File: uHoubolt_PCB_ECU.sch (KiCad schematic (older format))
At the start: 80 parts, among them J1 Power In, J2 Debug, J24 12V, J25 GND, J26 Servo, J3 CAN1, J35 CAN1, J36 CAN2, J37 CAN1, J38 CAN2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

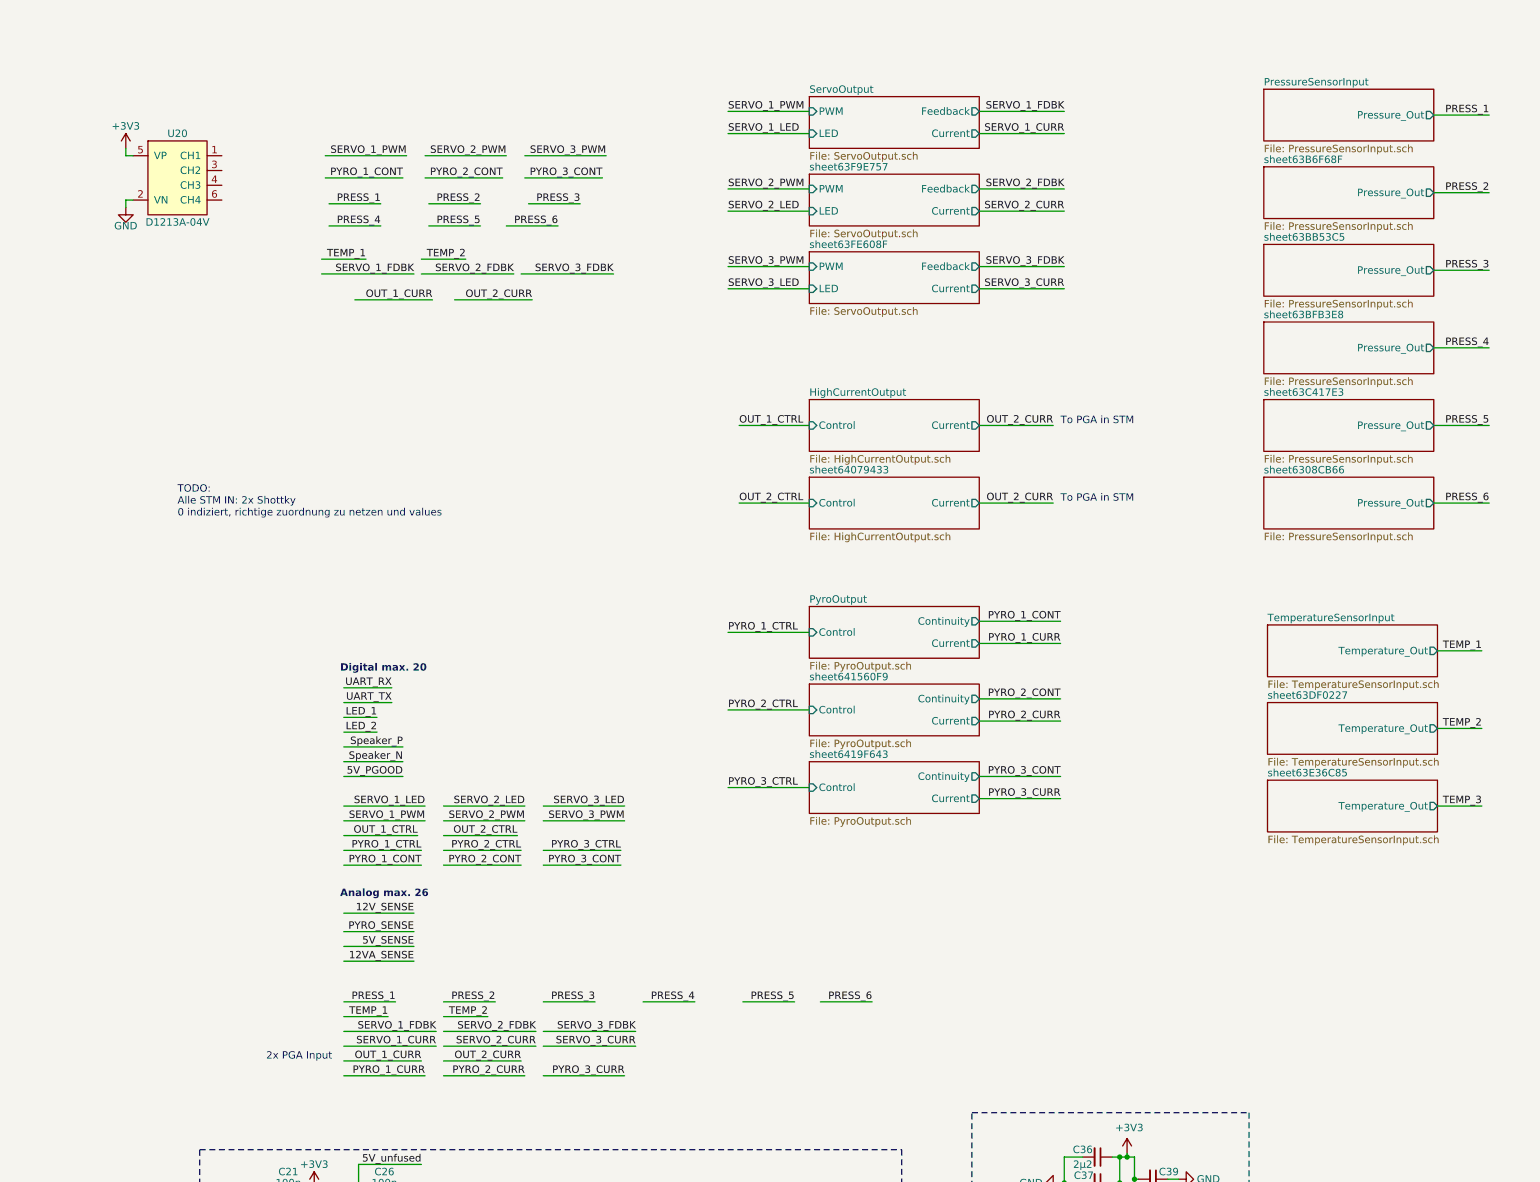
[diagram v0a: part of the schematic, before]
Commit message: fixed net names
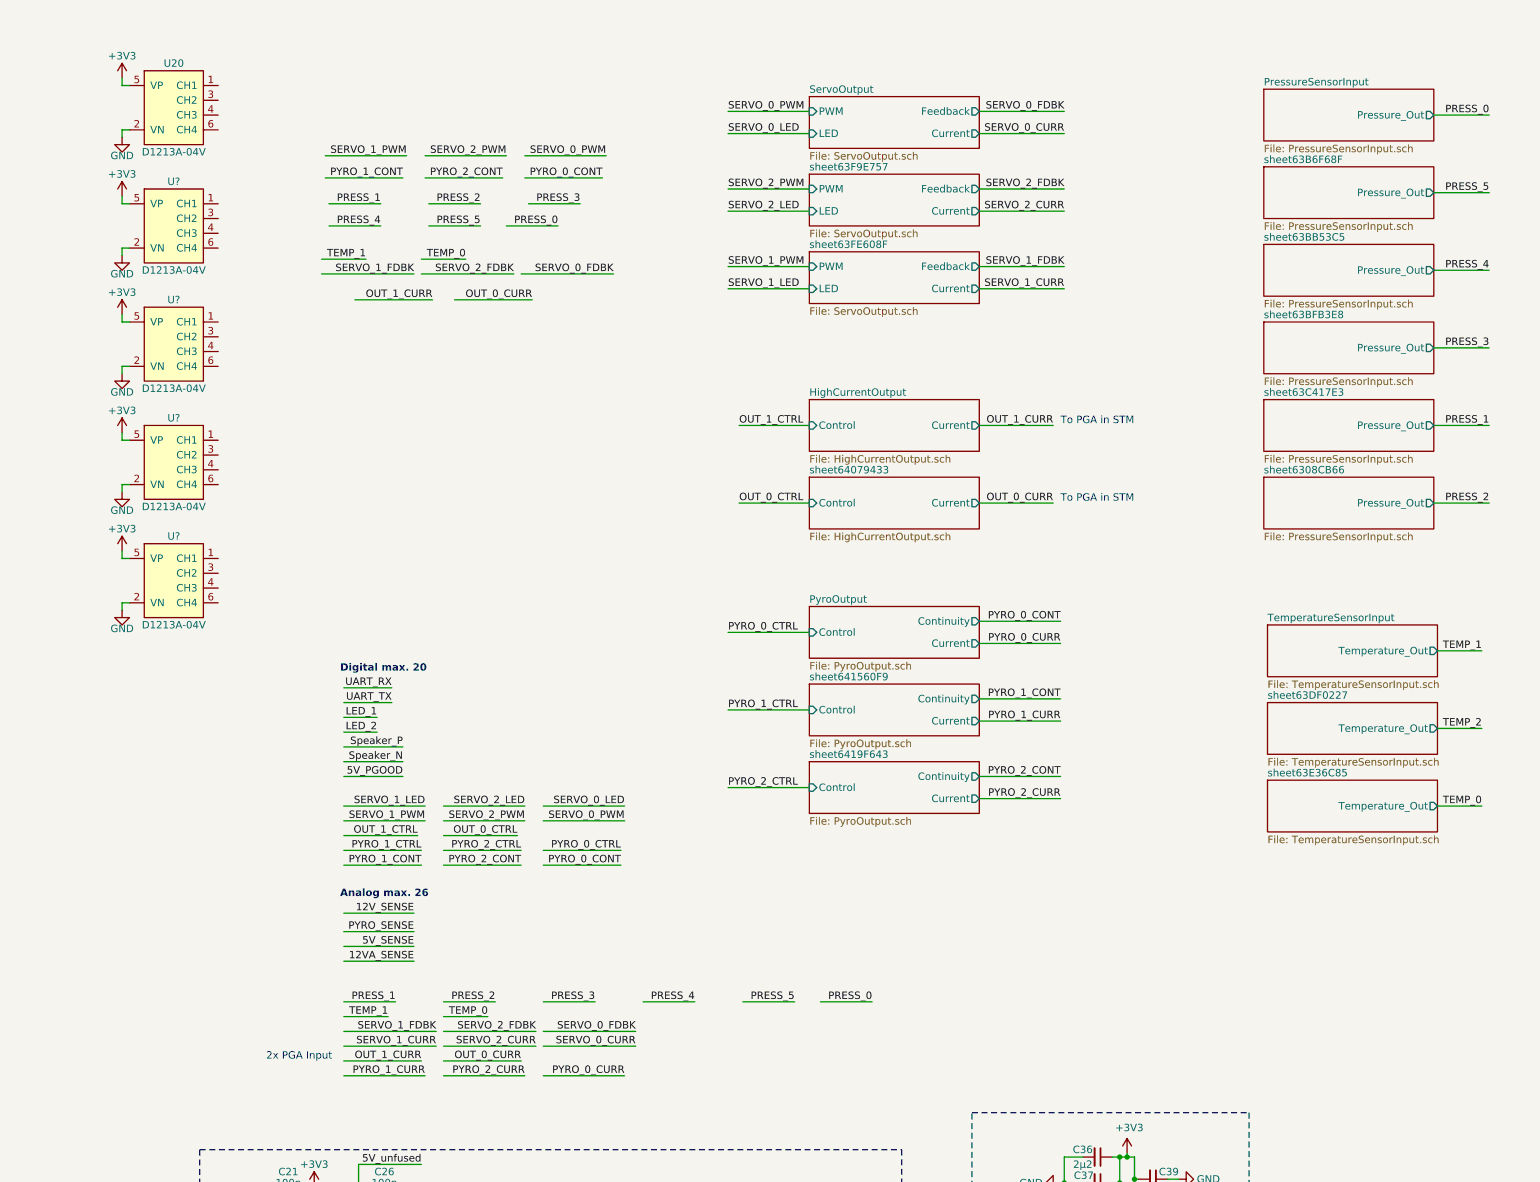
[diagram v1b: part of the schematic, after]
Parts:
- added U? (x4): D1213A-04V, Package_TO_SOT_SMD:SOT-563, symbol TXV_LIB:D1213A-04V
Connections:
- net labels added: OUT_0_CTRL, OUT_0_CURR, PRESS_0, PYRO_0_CONT, PYRO_0_CTRL, PYRO_0_CURR, SERVO_0_CURR, SERVO_0_FDBK, SERVO_0_LED, SERVO_0_PWM, TEMP_0
- net labels removed: OUT_2_CTRL, OUT_2_CURR, PRESS_6, PYRO_3_CONT, PYRO_3_CTRL, PYRO_3_CURR, SERVO_3_CURR, SERVO_3_FDBK, SERVO_3_LED, SERVO_3_PWM, TEMP_3
- wire segments 484 -> 500
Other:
- note removed: "TODO:\nAlle STM IN: 2x Shottky\n0 indiziert, richtige zuordnung zu netzen und values"
- moved on the sheet: U20

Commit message: schematic done, preliminary placement done
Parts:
- added Q3: SISA88DN or similar, TXV_LIB:PowerPAK_1212-8, symbol Device:Q_NMOS_GDS
- added R77: 120, Resistor_SMD:R_0603_1608Metric, symbol Device:R_Small
- added R78: 1k, Resistor_SMD:R_0603_1608Metric, symbol Device:R_Small
- gave numbers to parts that had none: 4
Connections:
- net labels added: SOLENOID_0_CTRL, SOLENOID_0_CURR, SOLENOID_1_CTRL, SOLENOID_1_CURR, Speaker
- net labels removed: OUT_0_CTRL, OUT_0_CURR, OUT_1_CTRL, OUT_1_CURR, Speaker_N, Speaker_P
- wire segments 500 -> 525
- no-connect marks 3 -> 5
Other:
- note added: "PGA"
- note added: "PGA Inverting In"
- note removed: "2x PGA Input"
- note removed: "Analog max. 26"
- note removed: "Digital max. 20"
- moved on the sheet: D4, D5, J2, LS1, R19, R20

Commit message: routing started
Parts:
- J1: footprint TXV_LIB:Molex_MegaFit_1x03_Vertical -> TXV_LIB:Molex_MegaFit_1x03_Vertical_Doublesided
- U20, U21, U22, U23, U24: footprint Package_TO_SOT_SMD:SOT-563 -> TXV_LIB:SOT-563
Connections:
- net +12V: now also LS1.1, R78.1
- net +12VA: no longer LS1.1, R78.1
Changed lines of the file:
@@
 F 0 "J1" H 775 1425 50  0000 C CNN
 F 1 "Power In" H 775 1350 50  0000 C CNN
-F 2 "TXV_LIB:Molex_MegaFit_1x03_Vertical" H 775 1150 50  0001 C CNN
+F 2 "TXV_LIB:Molex_MegaFit_1x03_Vertical_Doublesided" H 775 1150 50  0001 C CNN
 F 3 "~" H 775 1150 50  0001 C CNN
 	1    775  1150
@@
 F 0 "U20" H 6800 1500 50  0000 C CNN
 F 1 "D1213A-04V" H 6800 900 50  0000 C CNN
-F 2 "Package_TO_SOT_SMD:SOT-563" H 6800 800 50  0001 C CNN
+F 2 "TXV_LIB:SOT-563" H 6800 800 50  0001 C CNN
 F 3 "" H 6800 1200 50  0001 C CNN
 	1    6800 1200
@@
 F 0 "U21" H 6800 2300 50  0000 C CNN
 F 1 "D1213A-04V" H 6800 1700 50  0000 C CNN
-F 2 "Package_TO_SOT_SMD:SOT-563" H 6800 1600 50  0001 C CNN
+F 2 "TXV_LIB:SOT-563" H 6800 1600 50  0001 C CNN
 F 3 "" H 6800 2000 50  0001 C CNN
 	1    6800 2000
@@
 F 0 "U22" H 6800 3100 50  0000 C CNN
 F 1 "D1213A-04V" H 6800 2500 50  0000 C CNN
-F 2 "Package_TO_SOT_SMD:SOT-563" H 6800 2400 50  0001 C CNN
+F 2 "TXV_LIB:SOT-563" H 6800 2400 50  0001 C CNN
 F 3 "" H 6800 2800 50  0001 C CNN
 	1    6800 2800
@@
 F 0 "U23" H 6800 3900 50  0000 C CNN
 F 1 "D1213A-04V" H 6800 3300 50  0000 C CNN
-F 2 "Package_TO_SOT_SMD:SOT-563" H 6800 3200 50  0001 C CNN
+F 2 "TXV_LIB:SOT-563" H 6800 3200 50  0001 C CNN
 F 3 "" H 6800 3600 50  0001 C CNN
 	1    6800 3600
@@
 F 0 "U24" H 6800 4700 50  0000 C CNN
 F 1 "D1213A-04V" H 6800 4100 50  0000 C CNN
-F 2 "Package_TO_SOT_SMD:SOT-563" H 6800 4000 50  0001 C CNN
+F 2 "TXV_LIB:SOT-563" H 6800 4000 50  0001 C CNN
 F 3 "" H 6800 4400 50  0001 C CNN
 	1    6800 4400
@@
 	4475 4375 4525 4375
 $Comp
-L power:+12VA #PWR0228
-U 1 1 658F8B5D
-P 4475 4200
-F 0 "#PWR0228" H 4475 4050 50  0001 C CNN
-F 1 "+12VA" H 4475 4350 50  0000 C CNN
-F 2 "" H 4475 4200 50  0001 C CNN
-F 3 "" H 4475 4200 50  0001 C CNN
-	1    4475 4200
-	1    0    0    -1
-$EndComp
-$Comp
 L Device:R_Small R77
 U 1 1 6594F65C
@@
 	3050 1375 3050 1400
 Connection ~ 3050 1400
+$Comp
+L power:+12V #PWR?
+U 1 1 61D3A685
+P 4475 4200
+F 0 "#PWR?" H 4475 4050 50  0001 C CNN
+F 1 "+12V" H 4475 4350 50  0000 C CNN
+F 2 "" H 4475 4200 50  0001 C CNN
+F 3 "" H 4475 4200 50  0001 C CNN
+	1    4475 4200
+	1    0    0    -1
+$EndComp
 $EndSCHEMATC

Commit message: routing done, drc clean (3 errors to be ignored)
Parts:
- removed J24: 12V, TXV_LIB:PlatedEdgePad_6mm, symbol Connector_Generic:Conn_01x01
- removed J25: GND, TXV_LIB:PlatedEdgePad_6mm, symbol Connector_Generic:Conn_01x01
- removed J26: Servo, TXV_LIB:PlatedEdgePad_6mm, symbol Connector_Generic:Conn_01x01
- added JP2: Servo Voltage Select, TXV_LIB:Jumper3_6x2mm_Vias23, symbol Jumper:SolderJumper_3_Open
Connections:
- net +12V: now also JP2.2 (C)
- net GND: now also U8.9 (PAD), JP2.3 (B)
- net SOLENOID_0_CTRL: now also U6.48 (PD9); no longer U6.47 (PD8)
- net SOLENOID_0_CURR: now also U6.21 (PA7); no longer U6.24 (PB0)
- net SOLENOID_1_CTRL: now also U6.47 (PD8); no longer U6.48 (PD9)
- net SOLENOID_1_CURR: now also U6.24 (PB0); no longer U6.21 (PA7)
- net VS: now also JP2.1 (A)
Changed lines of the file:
@@
 L power:GND #PWR?
 U 1 1 63229F21
-P 3625 10750
+P 3625 10775
 AR Path="/6015C35D/63229F21" Ref="#PWR?"  Part="1"
 AR Path="/63229F21" Ref="#PWR052"  Part="1"
-F 0 "#PWR052" H 3625 10500 50  0001 C CNN
-F 1 "GND" H 3630 10577 50  0000 C CNN
-F 2 "" H 3625 10750 50  0001 C CNN
-F 3 "" H 3625 10750 50  0001 C CNN
-	1    3625 10750
+F 0 "#PWR052" H 3625 10525 50  0001 C CNN
+F 1 "GND" H 3630 10602 50  0000 C CNN
+F 2 "" H 3625 10775 50  0001 C CNN
+F 3 "" H 3625 10775 50  0001 C CNN
+	1    3625 10775
 	1    0    0    -1
 $EndComp
@@
 	2900 8925 2350 8925
 Wire Wire Line
-	5300 6925 4600 6925
-Text Label 5300 6925 2    50   ~ 0
+	5300 7025 4600 7025
+Text Label 5300 7025 2    50   ~ 0
 SOLENOID_1_CTRL
 Text Label 5125 7725 2    50   ~ 0
@@
 	2900 9025 2350 9025
 Wire Wire Line
-	5300 7025 4600 7025
-Text Label 5300 7025 2    50   ~ 0
+	5300 6925 4600 6925
+Text Label 5300 6925 2    50   ~ 0
 SOLENOID_0_CTRL
 Text Label 5125 7925 2    50   ~ 0
@@
 Text Label 5150 6725 2    50   ~ 0
 PYRO_2_CURR
-Text Label 2175 8125 0    50   ~ 0
-SOLENOID_0_CURR
 Wire Wire Line
 	2900 6925 2275 6925
@@
 L power:VS #PWR0101
 U 1 1 62FBA5C0
-P 3875 775
-F 0 "#PWR0101" H 3675 625 50  0001 C CNN
-F 1 "VS" H 3875 925 50  0000 C CNN
-F 2 "" H 3875 775 50  0001 C CNN
-F 3 "" H 3875 775 50  0001 C CNN
-	1    3875 775
-	1    0    0    -1
-$EndComp
-$Comp
-L power:+12V #PWR?
-U 1 1 62FBB19F
-P 3475 800
-AR Path="/61C7474C/62FBB19F" Ref="#PWR?"  Part="1"
-AR Path="/62FBB19F" Ref="#PWR0102"  Part="1"
-F 0 "#PWR0102" H 3475 650 50  0001 C CNN
-F 1 "+12V" H 3475 950 50  0000 C CNN
-F 2 "" H 3475 800 50  0001 C CNN
-F 3 "" H 3475 800 50  0001 C CNN
-	1    3475 800
+P 3925 750
+F 0 "#PWR0101" H 3725 600 50  0001 C CNN
+F 1 "VS" H 3925 900 50  0000 C CNN
+F 2 "" H 3925 750 50  0001 C CNN
+F 3 "" H 3925 750 50  0001 C CNN
+	1    3925 750
 	1    0    0    -1
 $EndComp
@@
 Wire Wire Line
 	6450 1350 6450 1400
-$Comp
-L Connector_Generic:Conn_01x01 J24
-U 1 1 63187D15
-P 3475 1025
-F 0 "J24" V 3375 1025 50  0000 L CNN
-F 1 "12V" V 3575 950 50  0000 L CNN
-F 2 "TXV_LIB:PlatedEdgePad_6mm" H 3475 1025 50  0001 C CNN
-F 3 "~" H 3475 1025 50  0001 C CNN
-	1    3475 1025
-	0    1    1    0
-$EndComp
-$Comp
-L Connector_Generic:Conn_01x01 J26
-U 1 1 6318DCA6
-P 3875 1025
-F 0 "J26" V 3825 825 50  0000 L CNN
-F 1 "Servo" V 3975 925 50  0000 L CNN
-F 2 "TXV_LIB:PlatedEdgePad_6mm" H 3875 1025 50  0001 C CNN
-F 3 "~" H 3875 1025 50  0001 C CNN
-	1    3875 1025
-	0    1    1    0
-$EndComp
-$Comp
-L Connector_Generic:Conn_01x01 J25
-U 1 1 6318E212
-P 3675 750
-F 0 "J25" V 3575 725 50  0000 R CNN
-F 1 "GND" V 3775 825 50  0000 R CNN
-F 2 "TXV_LIB:PlatedEdgePad_6mm" H 3675 750 50  0001 C CNN
-F 3 "~" H 3675 750 50  0001 C CNN
-	1    3675 750
-	0    -1   -1   0
-$EndComp
-$Comp
-L power:GND #PWR0208
-U 1 1 6318F78B
-P 3675 975
-F 0 "#PWR0208" H 3675 725 50  0001 C CNN
-F 1 "GND" H 3675 825 50  0000 C CNN
-F 2 "" H 3675 975 50  0001 C CNN
-F 3 "" H 3675 975 50  0001 C CNN
-	1    3675 975
-	-1   0    0    -1
-$EndComp
-Wire Wire Line
-	3475 800  3475 825
-Wire Wire Line
-	3675 950  3675 975
-Wire Wire Line
-	3875 775  3875 800
 Text Label 10550 1375 0    50   ~ 0
 SERVO_0_LED
@@
 Text Notes 3200 8350 0    50   ~ 0
 PGA Inverting In
-Wire Wire Line
-	2900 8125 2175 8125
-Wire Wire Line
-	2900 7225 2175 7225
-Text Label 2175 7225 0    50   ~ 0
-SOLENOID_1_CURR
 Text Notes 3200 7250 0    50   ~ 0
 PGA
@@
 L power:PWR_FLAG #FLG0103
 U 1 1 67327E1F
-P 4000 775
-F 0 "#FLG0103" H 4000 850 50  0001 C CNN
-F 1 "PWR_FLAG" H 4000 925 50  0000 C CNN
-F 2 "" H 4000 775 50  0001 C CNN
-F 3 "~" H 4000 775 50  0001 C CNN
-	1    4000 775
-	1    0    0    -1
-$EndComp
-Wire Wire Line
-	4000 775  4000 800
-Wire Wire Line
-	4000 800  3875 800
-Connection ~ 3875 800
-Wire Wire Line
-	3875 800  3875 825
+P 4025 750
+F 0 "#FLG0103" H 4025 825 50  0001 C CNN
+F 1 "PWR_FLAG" V 4100 750 50  0000 C CNN
+F 2 "" H 4025 750 50  0001 C CNN
+F 3 "~" H 4025 750 50  0001 C CNN
+	1    4025 750
+	1    0    0    -1
+$EndComp
 $Comp
 L power:PWR_FLAG #FLG0104
@@
 Connection ~ 3050 1400
 $Comp
-L power:+12V #PWR?
+L power:+12V #PWR0102
 U 1 1 61D3A685
 P 4475 4200
-F 0 "#PWR?" H 4475 4050 50  0001 C CNN
+F 0 "#PWR0102" H 4475 4050 50  0001 C CNN
 F 1 "+12V" H 4475 4350 50  0000 C CNN
 F 2 "" H 4475 4200 50  0001 C CNN
@@
 	1    0    0    -1
 $EndComp
+$Comp
+L Jumper:SolderJumper_3_Open JP2
+U 1 1 61C315C6
+P 3700 925
+F 0 "JP2" H 3700 1038 50  0000 C CNN
+F 1 "Servo Voltage Select" H 3700 1175 50  0000 C CNN
+F 2 "TXV_LIB:Jumper3_6x2mm_Vias23" H 3700 925 50  0001 C CNN
+F 3 "~" H 3700 925 50  0001 C CNN
+	1    3700 925
+	-1   0    0    1
+$EndComp
+$Comp
+L power:+12V #PWR?
+U 1 1 61D2D8D1
+P 3700 750
+AR Path="/61C7474C/61D2D8D1" Ref="#PWR?"  Part="1"
+AR Path="/61D2D8D1" Ref="#PWR0208"  Part="1"
+F 0 "#PWR0208" H 3700 600 50  0001 C CNN
+F 1 "+12V" H 3700 900 50  0000 C CNN
+F 2 "" H 3700 750 50  0001 C CNN
+F 3 "" H 3700 750 50  0001 C CNN
+	1    3700 750
+	1    0    0    -1
+$EndComp
+$Comp
+L power:GND #PWR0228
+U 1 1 61DC6265
+P 3475 950
+F 0 "#PWR0228" H 3475 700 50  0001 C CNN
+F 1 "GND" H 3475 800 50  0000 C CNN
+F 2 "" H 3475 950 50  0001 C CNN
+F 3 "" H 3475 950 50  0001 C CNN
+	1    3475 950
+	1    0    0    -1
+$EndComp
+Wire Wire Line
+	3475 950  3475 925
+Wire Wire Line
+	3475 925  3500 925
+Wire Wire Line
+	3700 750  3700 775
+Wire Wire Line
+	3925 750  3925 800
+Wire Wire Line
+	3925 925  3900 925
+Wire Wire Line
+	4025 750  4025 800
+Wire Wire Line
+	4025 800  3925 800
+Connection ~ 3925 800
+Wire Wire Line
+	3925 800  3925 925
+Wire Wire Line
+	2900 7225 2175 7225
+Text Label 2175 7225 0    50   ~ 0
+SOLENOID_0_CURR
+Text Label 2175 8125 0    50   ~ 0
+SOLENOID_1_CURR
+Wire Wire Line
+	2900 8125 2175 8125
+Wire Wire Line
+	3475 10725 3475 10750
+Wire Wire Line
+	3475 10750 3625 10750
+Connection ~ 3625 10750
+Wire Wire Line
+	3625 10750 3625 10775
 $EndSCHEMATC

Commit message: small improvements, updated doc
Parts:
- added G1: SpaceTeam_LOGO, TXV_LIB:ST_Logo_new, symbol TXV_LIB:SpaceTeam_LOGO
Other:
- note added: "I/O Protection"
- note added: "Inputs & Outputs"
- moved on the sheet: C10, C12, C16, C17, C18, C19, C20, C21, C22, C23, C25, C26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

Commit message: small changes, generated gerbers
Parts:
- U4: value MCP2562FDT-H_SN -> MCP2562FDx-x_MF
- U5: value MCP2562FDT -> MCP2562FDx-x_MF
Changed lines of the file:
@@
 AR Path="/6322A0B2" Ref="U5"  Part="1"
 F 0 "U5" H 9375 8475 50  0000 C CNN
-F 1 "MCP2562FDT" H 9550 8550 50  0000 C CNN
+F 1 "MCP2562FDx-x_MF" H 9675 8550 50  0000 C CNN
 F 2 "Package_DFN_QFN:DFN-8-1EP_3x3mm_P0.65mm_EP1.55x2.4mm" H 9175 8400 50  0001 C CIN
 F 3 "http://ww1.microchip.com/downloads/en/DeviceDoc/25167A.pdf" H 9175 8900 50  0001 C CNN
@@
 AR Path="/6015C35D/6322A030" Ref="U?"  Part="1"
 AR Path="/6322A030" Ref="U4"  Part="1"
-F 0 "U4" H 9250 7000 50  0000 C CNN
-F 1 "MCP2562FDT-H_SN" H 9575 7100 50  0000 C CNN
+F 0 "U4" H 9350 7050 50  0000 C CNN
+F 1 "MCP2562FDx-x_MF" H 9650 7125 50  0000 C CNN
 F 2 "Package_DFN_QFN:DFN-8-1EP_3x3mm_P0.65mm_EP1.55x2.4mm" H 9175 6975 50  0001 C CIN
 F 3 "http://ww1.microchip.com/downloads/en/DeviceDoc/25167A.pdf" H 9175 7475 50  0001 C CNN

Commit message: some more small changes
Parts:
- R12, R4, R8: value 9k1 -> 56k
- R13, R5, R9: value 1k -> 10k
- R14, R15, R16: value 9k1 -> 10k
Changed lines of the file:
@@
 AR Path="/63229E9D" Ref="R16"  Part="1"
 F 0 "R16" V 1625 5350 50  0000 C CNN
-F 1 "9k1" V 1700 5350 50  0000 C CNN
+F 1 "10k" V 1700 5350 50  0000 C CNN
 F 2 "Resistor_SMD:R_0603_1608Metric" H 1775 5350 50  0001 C CNN
 F 3 "~" H 1775 5350 50  0001 C CNN
@@
 P 6325 2900
 F 0 "#FLG0102" H 6325 2975 50  0001 C CNN
-F 1 "PWR_FLAG" H 6325 3050 50  0000 C CNN
+F 1 "PWR_FLAG" V 6400 2975 50  0000 C CNN
 F 2 "" H 6325 2900 50  0001 C CNN
 F 3 "~" H 6325 2900 50  0001 C CNN
@@
 AR Path="/61C7474C/63A4C22D" Ref="#PWR?"  Part="1"
 F 0 "#PWR0218" H 9775 2100 50  0001 C CNN
-F 1 "+3V3" H 9790 2423 50  0000 C CNN
+F 1 "+3V3" H 9775 2400 50  0000 C CNN
 F 2 "" H 9775 2250 50  0001 C CNN
 F 3 "" H 9775 2250 50  0001 C CNN
@@
 U 1 1 635C8D87
 P 6225 3125
-F 0 "R12" H 6075 3175 50  0000 L CNN
-F 1 "9k1" H 6050 3100 50  0000 L CNN
+F 0 "R12" H 6050 3175 50  0000 L CNN
+F 1 "56k" H 6050 3100 50  0000 L CNN
 F 2 "Resistor_SMD:R_0603_1608Metric" H 6225 3125 50  0001 C CNN
 F 3 "~" H 6225 3125 50  0001 C CNN
@@
 U 1 1 635C8D81
 P 6225 3425
-F 0 "R13" H 6075 3450 50  0000 L CNN
-F 1 "1k" H 6075 3375 50  0000 L CNN
+F 0 "R13" H 6050 3450 50  0000 L CNN
+F 1 "10k" H 6075 3375 50  0000 L CNN
 F 2 "Resistor_SMD:R_0603_1608Metric" H 6225 3425 50  0001 C CNN
 F 3 "~" H 6225 3425 50  0001 C CNN
@@
 P 6950 1125
 F 0 "R4" H 6800 1175 50  0000 L CNN
-F 1 "9k1" H 6775 1100 50  0000 L CNN
+F 1 "56k" H 6775 1100 50  0000 L CNN
 F 2 "Resistor_SMD:R_0603_1608Metric" H 6950 1125 50  0001 C CNN
 F 3 "~" H 6950 1125 50  0001 C CNN
@@
 P 6950 1425
 F 0 "R5" H 6800 1450 50  0000 L CNN
-F 1 "1k" H 6800 1375 50  0000 L CNN
+F 1 "10k" H 6750 1375 50  0000 L CNN
 F 2 "Resistor_SMD:R_0603_1608Metric" H 6950 1425 50  0001 C CNN
 F 3 "~" H 6950 1425 50  0001 C CNN
@@
 P 7800 1125
 F 0 "R8" H 7650 1175 50  0000 L CNN
-F 1 "9k1" H 7625 1100 50  0000 L CNN
+F 1 "56k" H 7625 1100 50  0000 L CNN
 F 2 "Resistor_SMD:R_0603_1608Metric" H 7800 1125 50  0001 C CNN
 F 3 "~" H 7800 1125 50  0001 C CNN
@@
 P 7800 1425
 F 0 "R9" H 7650 1450 50  0000 L CNN
-F 1 "1k" H 7650 1375 50  0000 L CNN
+F 1 "10k" H 7600 1375 50  0000 L CNN
 F 2 "Resistor_SMD:R_0603_1608Metric" H 7800 1425 50  0001 C CNN
 F 3 "~" H 7800 1425 50  0001 C CNN
@@
 P 9025 2675
 F 0 "R14" H 8825 2725 50  0000 L CNN
-F 1 "9k1" H 8825 2650 50  0000 L CNN
+F 1 "10k" H 8825 2650 50  0000 L CNN
 F 2 "Resistor_SMD:R_0603_1608Metric" H 9025 2675 50  0001 C CNN
 F 3 "~" H 9025 2675 50  0001 C CNN
@@
 P 9025 2925
 F 0 "R15" H 8825 2950 50  0000 L CNN
-F 1 "9k1" H 8825 2875 50  0000 L CNN
+F 1 "10k" H 8825 2875 50  0000 L CNN
 F 2 "Resistor_SMD:R_0603_1608Metric" H 9025 2925 50  0001 C CNN
 F 3 "~" H 9025 2925 50  0001 C CNN
